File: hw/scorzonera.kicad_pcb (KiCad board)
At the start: 2 copper layers, 70.7 x 53.3 mm, 30 parts, among them J1 NEIGHBOR1, J2 NEIGHBOR2, J3 Conn_01x05, J7 BONUS_ROW, U1 AM7969, U3 MAX3232, U4 TXS0108EPW, U5 TXS0108EPW, Y1 Crystal_GND24

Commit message: Fiducials
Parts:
- added FD1: Fiducial_1mm_Dia_2mm_Outer, Fiducial:Fiducial_1mm_Dia_2mm_Outer, F.Cu at (115.5, 80.0)
- added FD2: Fiducial_1mm_Dia_2mm_Outer, Fiducial:Fiducial_1mm_Dia_2mm_Outer, F.Cu at (115.5, 110.0)
- added FD3: Fiducial_1mm_Dia_2mm_Outer, Fiducial:Fiducial_1mm_Dia_2mm_Outer, F.Cu at (176.5, 80.0)
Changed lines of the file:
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@@
     (tracks 348)
     (zones 0)
-    (modules 30)
+    (modules 33)
     (nets 134)
   )
@@
     (add_net /VLTN)
   )
+  (module Fiducial:Fiducial_1mm_Dia_2mm_Outer (layer F.Cu)
+    (at 176.5 80)
+    (descr "Circular Fiducial, 1mm bare copper top, 2mm keepout (Level A)")
+    (tags fiducial)
+    (attr smd)
+    (fp_text reference FD3 (at -2.85 0) (layer F.SilkS) hide
+      (effects (font (size 1 1) (thickness 0.15)))
+    )
+    (fp_text value Fiducial_1mm_Dia_2mm_Outer (at 0 2) (layer F.Fab)
+      (effects (font (size 1 1) (thickness 0.15)))
+    )
+    (fp_circle (center 0 0) (end 1 0) (layer F.Fab) (width 0.1))
+    (fp_text user %R (at 0 0) (layer F.Fab)
+      (effects (font (size 0.4 0.4) (thickness 0.06)))
+    )
+    (fp_circle (center 0 0) (end 1.25 0) (layer F.CrtYd) (width 0.05))
+    (pad "" smd circle (at 0 0) (size 1 1) (layers F.Cu F.Mask)
+      (solder_mask_margin 0.5) (clearance 0.5))
+  )
+  (module Fiducial:Fiducial_1mm_Dia_2mm_Outer (layer F.Cu)
+    (at 115.55 110)
+    (descr "Circular Fiducial, 1mm bare copper top, 2mm keepout (Level A)")
+    (tags fiducial)
+    (attr smd)
+    (fp_text reference FD2 (at 0 -2) (layer F.SilkS) hide
+      (effects (font (size 1 1) (thickness 0.15)))
+    )
+    (fp_text value Fiducial_1mm_Dia_2mm_Outer (at 0 2) (layer F.Fab)
+      (effects (font (size 1 1) (thickness 0.15)))
+    )
+    (fp_circle (center 0 0) (end 1 0) (layer F.Fab) (width 0.1))
+    (fp_text user %R (at 0 0) (layer F.Fab)
+      (effects (font (size 0.4 0.4) (thickness 0.06)))
+    )
+    (fp_circle (center 0 0) (end 1.25 0) (layer F.CrtYd) (width 0.05))
+    (pad "" smd circle (at 0 0) (size 1 1) (layers F.Cu F.Mask)
+      (solder_mask_margin 0.5) (clearance 0.5))
+  )
   (module wago:Texas_R-PVQFN-N20_4.65x3.65x1mm (layer F.Cu)
     (at 133.15 106.325)
@@
     )
   )
+  (module Fiducial:Fiducial_1mm_Dia_2mm_Outer (layer F.Cu)
+    (at 115.55 80)
+    (descr "Circular Fiducial, 1mm bare copper top, 2mm keepout (Level A)")
+    (tags fiducial)
+    (attr smd)
+    (fp_text reference FD1 (at -2.85 0) (layer F.SilkS) hide
+      (effects (font (size 1 1) (thickness 0.15)))
+    )
+    (fp_text value Fiducial_1mm_Dia_2mm_Outer (at 0 2) (layer F.Fab)
+      (effects (font (size 1 1) (thickness 0.15)))
+    )
+    (fp_circle (center 0 0) (end 1.25 0) (layer F.CrtYd) (width 0.05))
+    (fp_text user %R (at 0 0) (layer F.Fab)
+      (effects (font (size 0.4 0.4) (thickness 0.06)))
+    )
+    (fp_circle (center 0 0) (end 1 0) (layer F.Fab) (width 0.1))
+    (pad "" smd circle (at 0 0) (size 1 1) (layers F.Cu F.Mask)
+      (solder_mask_margin 0.5) (clearance 0.5))
+  )
+  (gr_text https://flomp.net/scorzonera (at 168.7 110.1) (layer F.SilkS)
+    (effects (font (size 1.016 0.762) (thickness 0.1524)))
+  )
   (gr_text MW (at 176.5 77.2) (layer F.SilkS)
     (effects (font (size 1.5 1.5) (thickness 0.3)))
@@
     (effects (font (size 3.048 2.54) (thickness 0.4572)))
   )
-  (gr_text https://flomp.net/scorzonera (at 168.7 110.1) (layer F.SilkS)
-    (effects (font (size 1.016 0.762) (thickness 0.1524)))
-  )
   (gr_line (start 109.6772 98.933) (end 109.728 99.9998) (angle 90) (layer Edge.Cuts) (width 0.15))

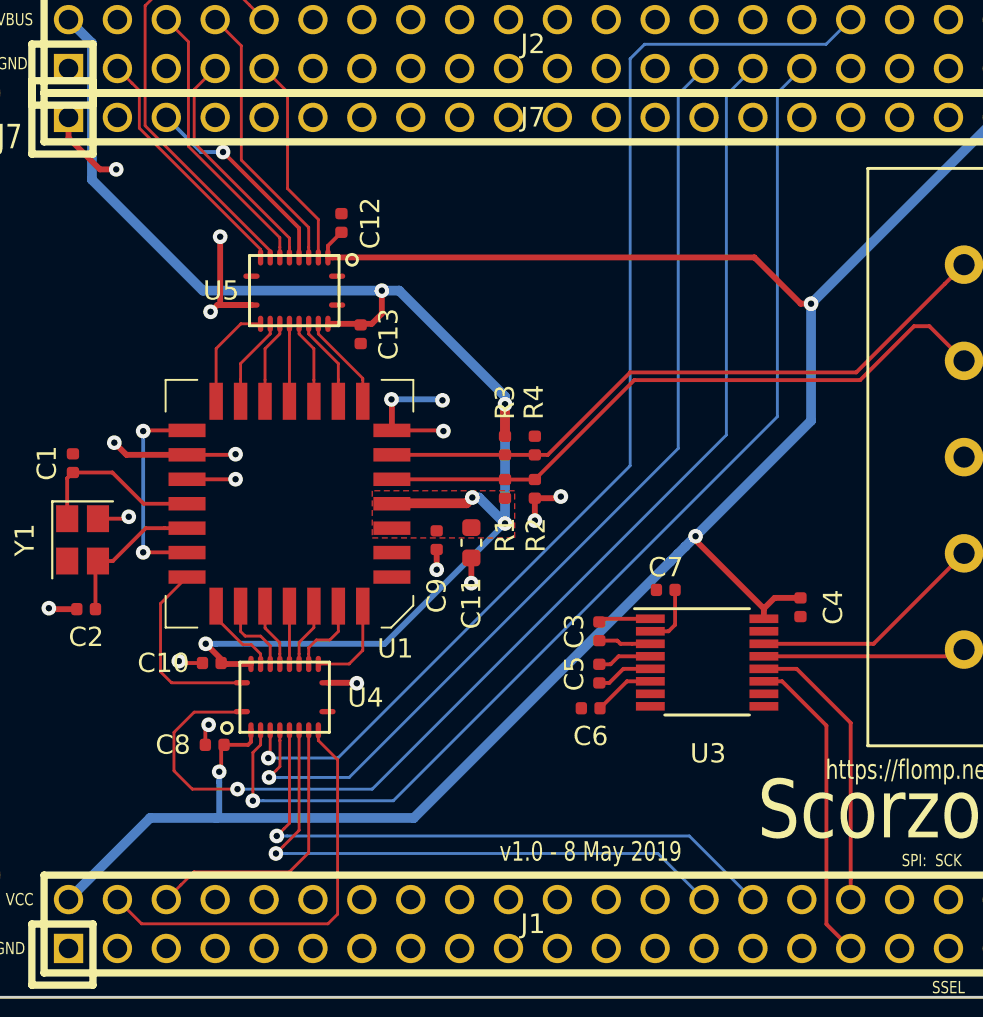
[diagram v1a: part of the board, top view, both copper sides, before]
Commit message: Connect OEs & add pulldowns, more silk, random cleanup
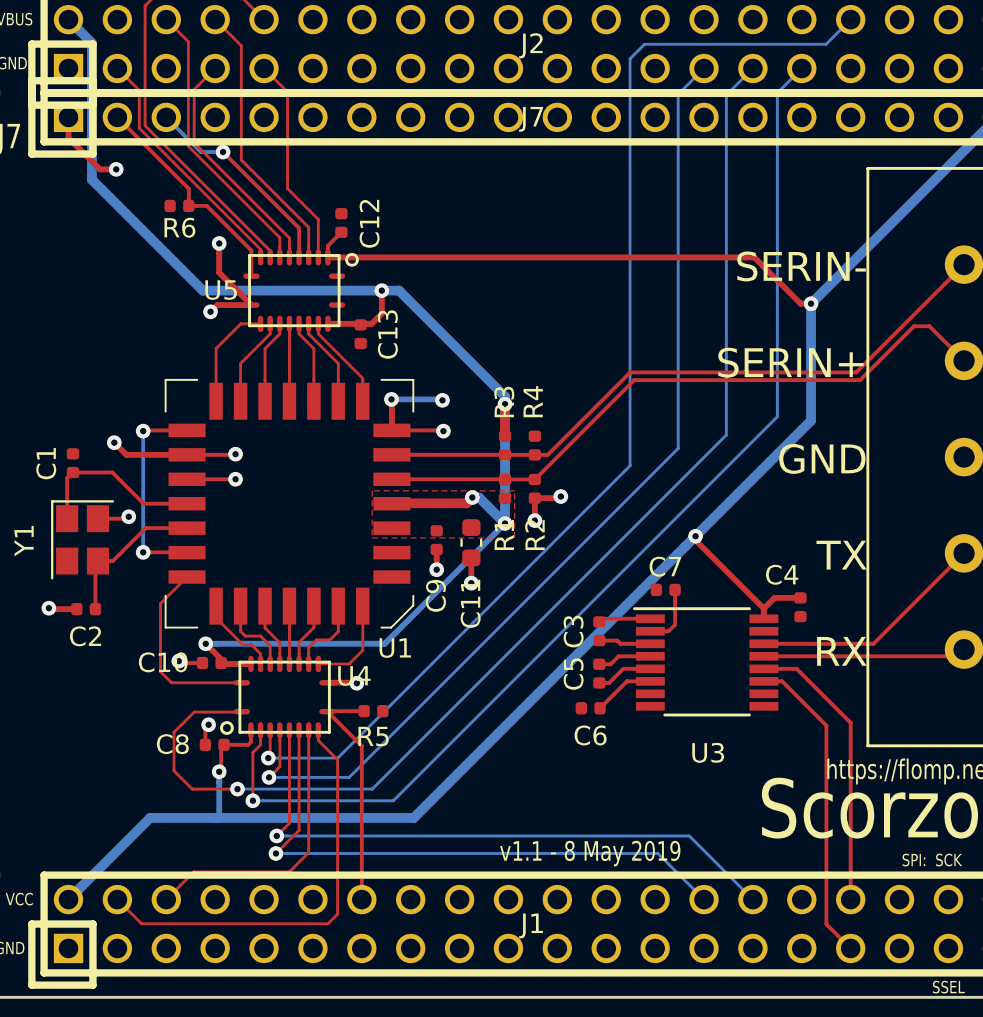
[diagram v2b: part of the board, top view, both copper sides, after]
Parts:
- added R5: 10K, Resistor_SMD:R_0402_1005Metric, F.Cu at (137.8, 107.0)
- added R6: 10K, Resistor_SMD:R_0402_1005Metric, F.Cu at (127.7, 80.8)
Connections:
- U3 pad 10: Net-(U3-Pad10) -> GND
- U3 pad 8: Net-(U3-Pad8) -> GND
- U4 pad 10: Net-(U4-Pad10) -> /P5_2
- U5 pad 10: Net-(U5-Pad10) -> /P6_4
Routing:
- net /P5_2: track 0.00 -> 12.4 mm
- net /P6_4: track 0.00 -> 11.7 mm
- net GND: track 39.7 -> 38.4 mm
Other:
- board text added: "RX"
- board text added: "SERIN+"
- board text added: "SERIN-"
- board text added: "TX"
- board text added: "v1.1 - 8 May 2019"
- board text removed: "v1.0 - 8 May 2019"
